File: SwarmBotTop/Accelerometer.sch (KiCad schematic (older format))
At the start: 3 parts, among them U4 LIS2DH

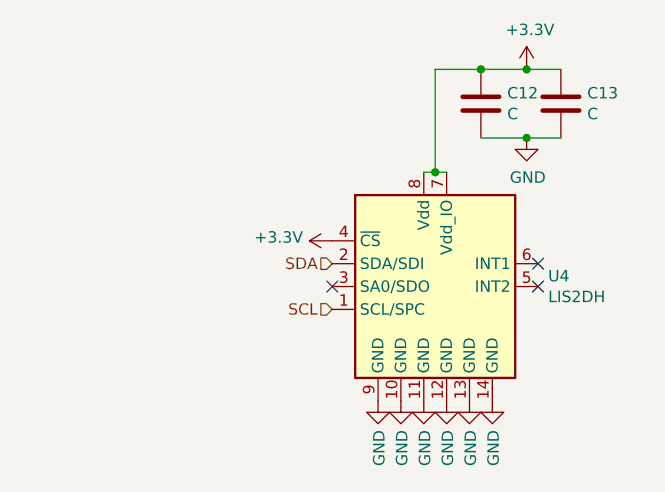
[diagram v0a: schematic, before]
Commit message: Camera routing with all sensors and motors
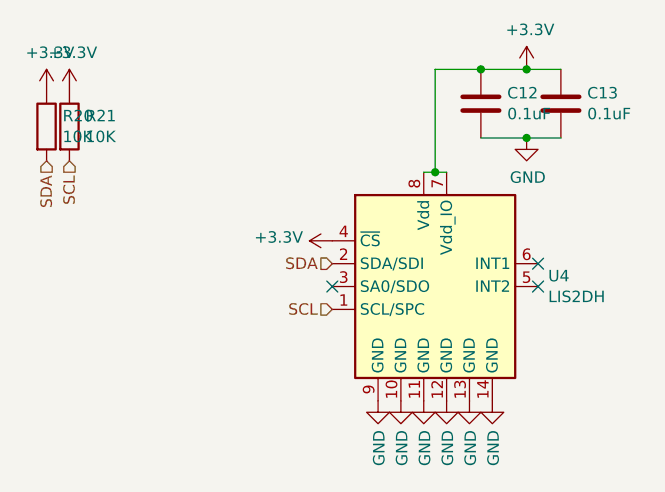
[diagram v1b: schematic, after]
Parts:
- added R20, R21: 10K, Resistor_SMD:R_0402_1005Metric, symbol Device:R
- C12, C13: value C -> 0.1uF
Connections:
- net +3V3: now also R20.1, R21.1
- net SCL: now also R21.2
- net SDA: now also R20.2
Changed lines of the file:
@@
 AR Path="/5DAF9EB1/5DE7582A/5DE767FA" Ref="C12"  Part="1"
 F 0 "C12" H 7615 2646 50  0000 L CNN
-F 1 "C" H 7615 2555 50  0000 L CNN
+F 1 "0.1uF" H 7615 2555 50  0000 L CNN
 F 2 "Capacitor_SMD:C_0402_1005Metric" H 7538 2450 50  0001 C CNN
 F 3 "~" H 7500 2600 50  0001 C CNN
@@
 AR Path="/5DAF9EB1/5DE7582A/5DE76801" Ref="C13"  Part="1"
 F 0 "C13" H 7965 2646 50  0000 L CNN
-F 1 "C" H 7965 2555 50  0000 L CNN
+F 1 "0.1uF" H 7965 2555 50  0000 L CNN
 F 2 "Capacitor_SMD:C_0402_1005Metric" H 7888 2450 50  0001 C CNN
 F 3 "~" H 7850 2600 50  0001 C CNN
@@
 NoConn ~ 7750 3300
 NoConn ~ 7750 3400
+Text HLabel 5600 2850 3    50   Input ~ 0
+SDA
+Text HLabel 5700 2850 3    50   Input ~ 0
+SCL
+$Comp
+L Device:R R21
+U 1 1 5DF1ADEB
+P 5700 2700
+F 0 "R21" H 5770 2746 50  0000 L CNN
+F 1 "10K" H 5770 2655 50  0000 L CNN
+F 2 "Resistor_SMD:R_0402_1005Metric" V 5630 2700 50  0001 C CNN
+F 3 "~" H 5700 2700 50  0001 C CNN
+	1    5700 2700
+	1    0    0    -1
+$EndComp
+$Comp
+L Device:R R20
+U 1 1 5DF1B0C7
+P 5600 2700
+F 0 "R20" H 5670 2746 50  0000 L CNN
+F 1 "10K" H 5670 2655 50  0000 L CNN
+F 2 "Resistor_SMD:R_0402_1005Metric" V 5530 2700 50  0001 C CNN
+F 3 "~" H 5600 2700 50  0001 C CNN
+	1    5600 2700
+	1    0    0    -1
+$EndComp
+$Comp
+L power:+3.3V #PWR0186
+U 1 1 5DF1BC69
+P 5600 2550
+F 0 "#PWR0186" H 5600 2400 50  0001 C CNN
+F 1 "+3.3V" H 5615 2723 50  0000 C CNN
+F 2 "" H 5600 2550 50  0001 C CNN
+F 3 "" H 5600 2550 50  0001 C CNN
+	1    5600 2550
+	1    0    0    -1
+$EndComp
+$Comp
+L power:+3.3V #PWR0187
+U 1 1 5DF1BDDF
+P 5700 2550
+F 0 "#PWR0187" H 5700 2400 50  0001 C CNN
+F 1 "+3.3V" H 5715 2723 50  0000 C CNN
+F 2 "" H 5700 2550 50  0001 C CNN
+F 3 "" H 5700 2550 50  0001 C CNN
+	1    5700 2550
+	1    0    0    -1
+$EndComp
 $EndSCHEMATC
